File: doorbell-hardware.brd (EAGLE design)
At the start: 100 x 80 mm, 14 parts, among them T1 BC846

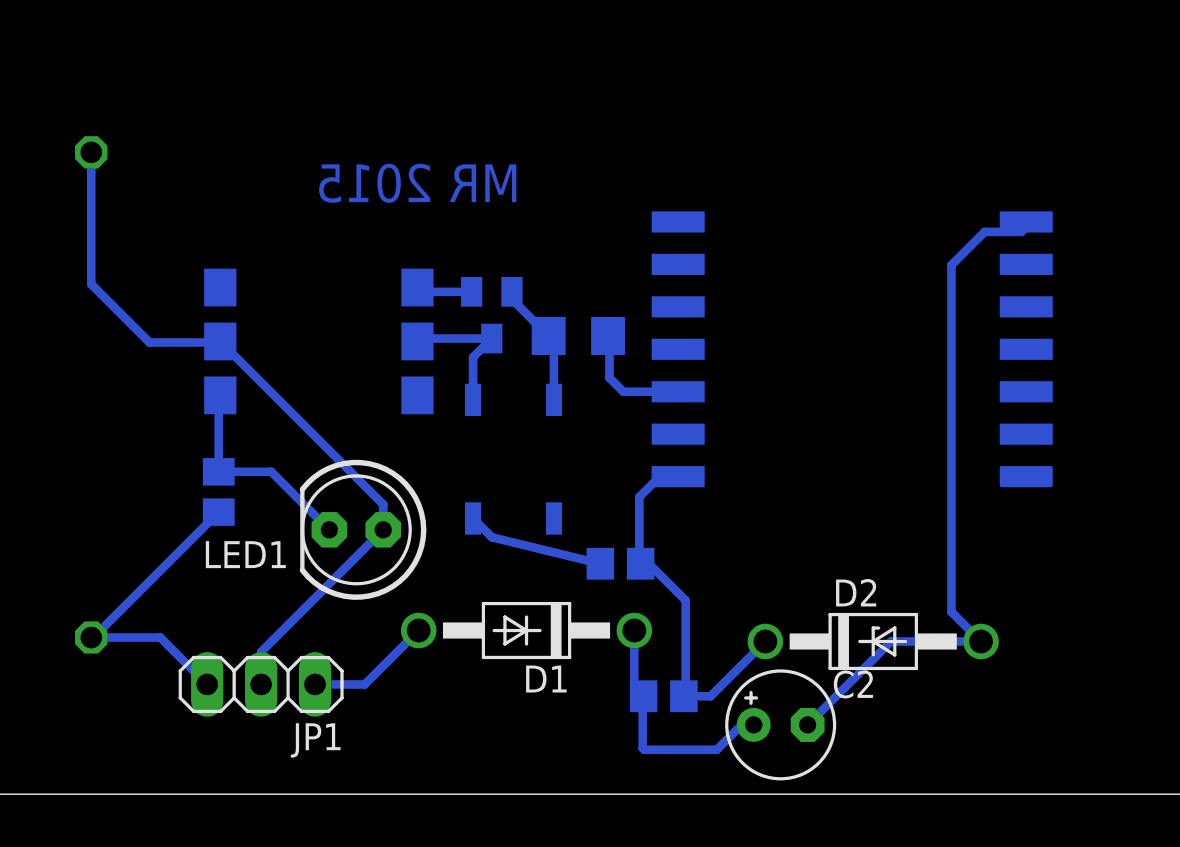
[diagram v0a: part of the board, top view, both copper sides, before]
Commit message: Replaced zener with ldo, started work on sleep and interrupt
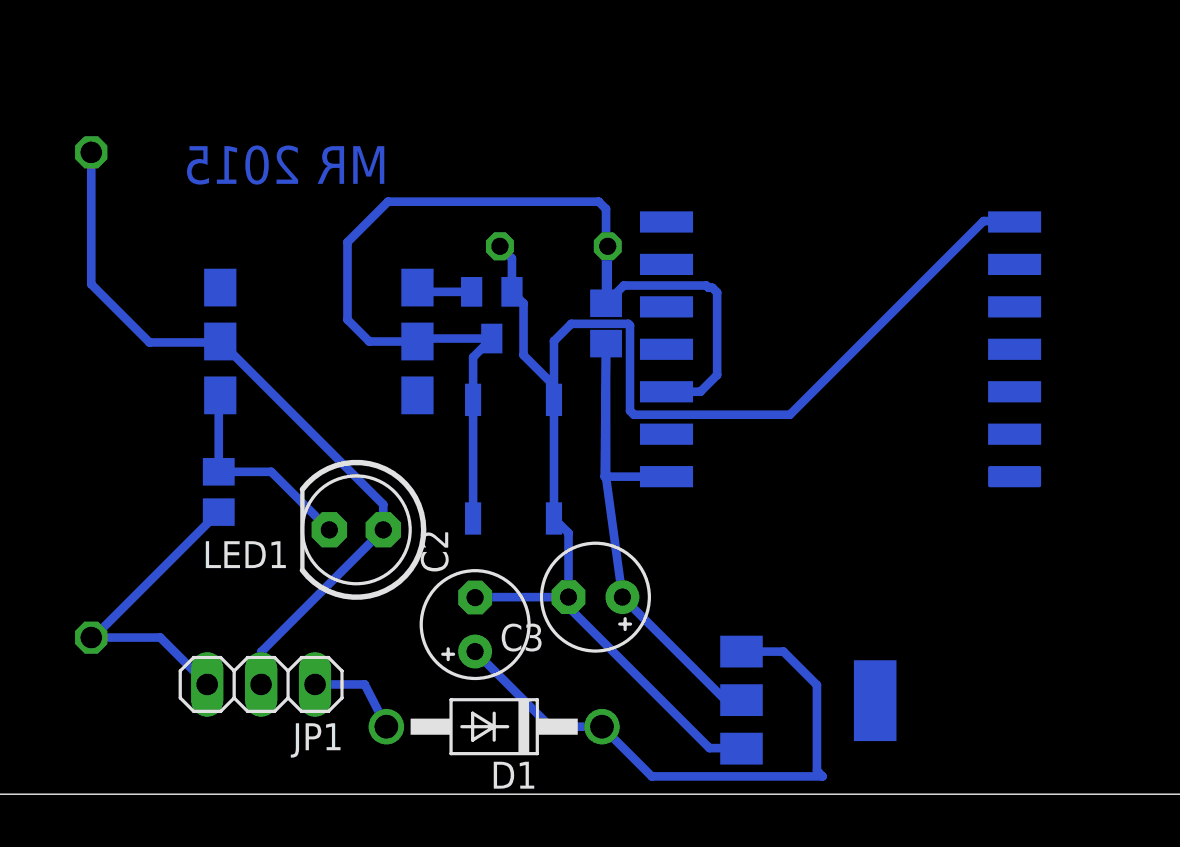
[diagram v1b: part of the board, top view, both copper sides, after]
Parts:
- removed D2: 1N4728, diode:DO41Z10
- removed R2: (no value), eagle-ltspice:R0805
- added C3: 100u, rcl:E2,5-5
- added IC1: REG1117, burr-brown:SOT223
- C1: value (none) -> 10u; device rcl:C1206 -> rcl:C050-024X044
- C2: value (none) -> 10u
- R4: value 1k -> 10k
- moved C2 15.2 mm to (23.7, 7.99), turned to 90 degrees
- moved R4 11.3 mm to (29.9, 22.2), turned to 270 degrees
- moved D1 4.78 mm to (24.6, 3.18)
- moved C1 4.38 mm to (27.4, 25.8)
- moved U$1 0.55 mm to (40.9, 21.8)
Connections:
- removed net N$5: OK1.5, R4.1, S1.3, S1.4, T1.3
- removed net N$6: C1.1, S1.1, S1.2, T1.2
- net BUTTON: now also OK1.5, R4.1, S1.3, S1.4, T1.3
- net GND: now also C1.1, C3.-, IC1.1, S1.1, S1.2, T1.2; no longer D2.A
- net N$1: now also IC1.3; no longer R2.2
- net VCC: now also C3.+, IC1.2; no longer D2.C, R2.1
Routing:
- net BUTTON: track 5.51 -> 52.7 mm
- net GND: track 32.6 -> 66.4 mm
- net N$1: track 11.5 -> 27.4 mm
- net N$5: track 13.3 -> 0.00 mm
- net VCC: track 17.9 -> 28.8 mm
- net N$6: track 5.91 -> 0.00 mm
- net AC+: track 5.94 -> 4.58 mm

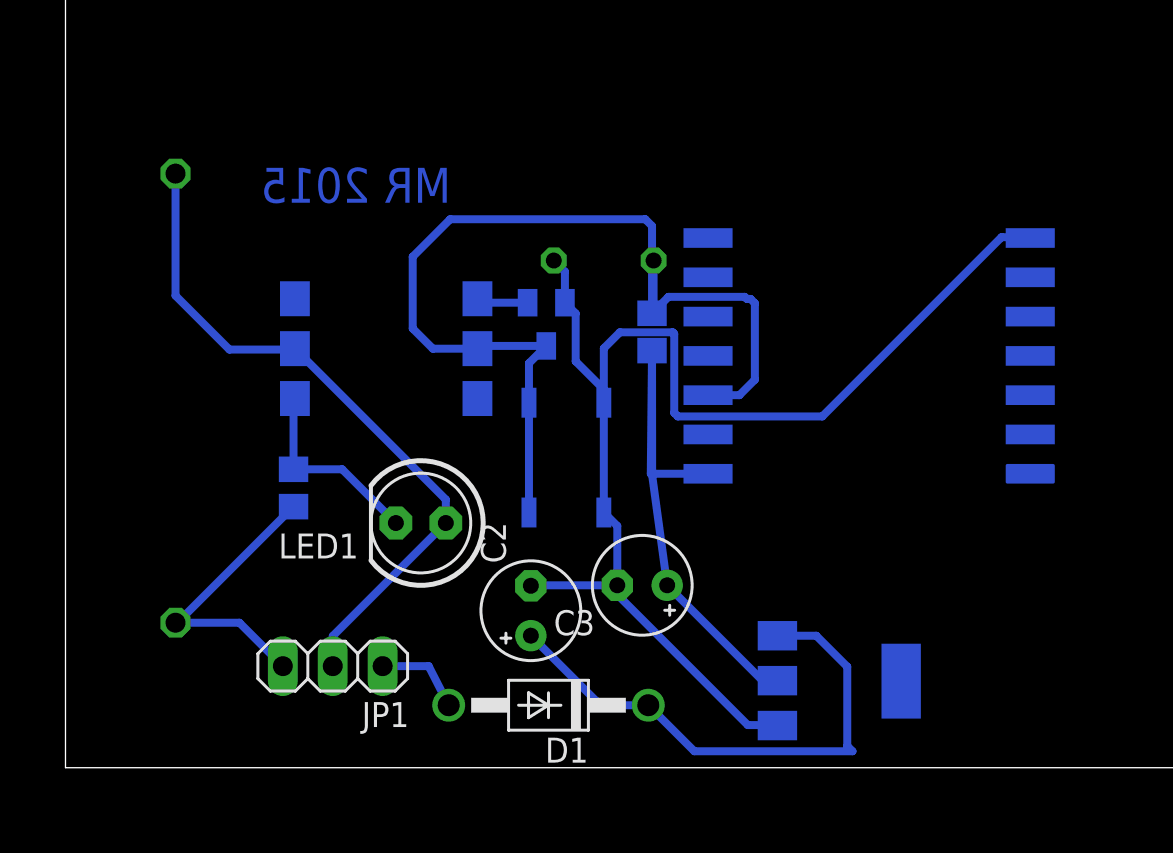
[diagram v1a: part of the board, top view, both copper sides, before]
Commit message: simplified circuit and code
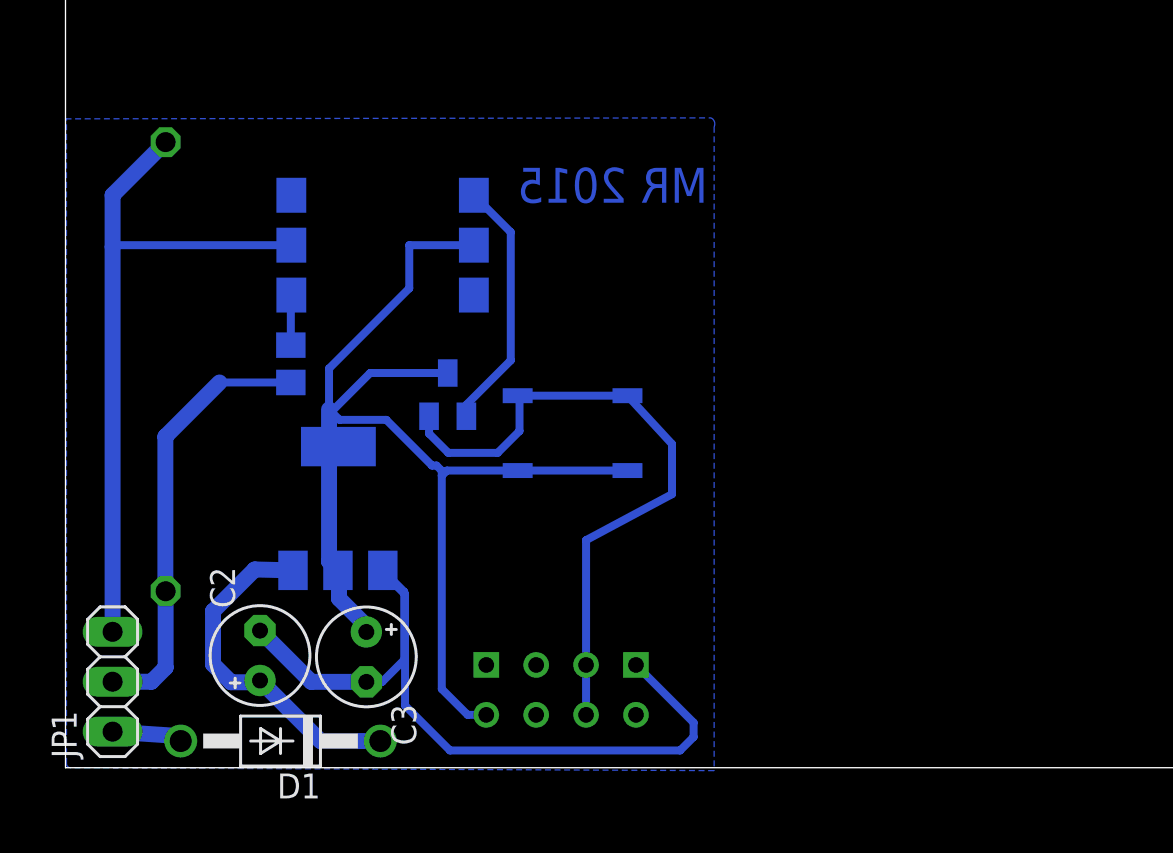
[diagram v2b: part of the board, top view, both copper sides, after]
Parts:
- removed C1: 10u, rcl:C050-024X044
- removed LED1: (no value), adafruit:LED5MM
- removed R4: 10k, eagle-ltspice:R0805
- U$1: value ESP07 -> ESP01; device esp8266modules:ESP07 -> esp8266modules:ESP01
- moved IC1 27.0 mm to (13.9, 13.2), turned to 0 degrees
- moved U$1 19.1 mm to (25.2, 10.9), turned to 0 degrees
- moved C3 14.5 mm to (15.3, 5.64), turned to 270 degrees
- moved C2 14.0 mm to (9.90, 5.71)
- moved D1 13.8 mm to (10.9, 1.36)
- moved JP1 11.2 mm to (2.40, 4.38), turned to 90 degrees
- moved R3 6.32 mm to (11.5, 20.6)
- moved T1 6.16 mm to (19.5, 19.0), turned to 0 degrees
- moved OK1 5.27 mm to (16.1, 26.6)
- moved R1 1.68 mm to (5.10, 20.4)
- moved S1 1.28 mm to (25.8, 17.0), turned to 0 degrees
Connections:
- net AC-: now also JP1.2; no longer JP1.3
- net BUTTON: now also S1.1, S1.2, T1.2, U$1.CH_PD, U$1.GPIO2; no longer C1.2, OK1.5, R4.1, S1.3, S1.4, T1.3, U$1.GPIO12
- net GND: no longer C1.1, S1.1, S1.2, T1.2
- net N$2: now also JP1.3; no longer JP1.2, LED1.A
- net N$3: no longer LED1.K
- net VCC: now also OK1.5, S1.3, S1.4, T1.3; no longer R4.2
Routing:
- net VCC: track 28.8 -> 62.7 mm
- net GND: track 66.4 -> 42.0 mm
- net BUTTON: track 52.7 -> 33.5 mm
- net N$4: track 2.64 -> 13.0 mm
- net N$1: track 27.4 -> 17.9 mm
- net AC-: track 14.8 -> 22.8 mm
- net N$3: track 9.97 -> 2.56 mm
- net AC+: track 4.58 -> 3.84 mm
- added copper zone on layer 16, net N$5

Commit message: Working schematic and smaller layout
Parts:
- removed C3: 100u, rcl:E2,5-5
- removed IC1: REG1117, burr-brown:SOT223
- removed S1: TAC_SWITCHSMD, SparkFun-Electromechanical:TACTILE-SWITCH-SMD
- added C1: 220u, resistor:E2-4
- added D2: 1N4148DO35-7, diode:DO35-7
- added JP2: (no value), pinhead:1X02
- added R2: 1.2k, resistor:0204/5
- C2: value 10u -> 0.1u; device rcl:E2,5-5 -> capacitor-wima:C2.5-2
- D1: value 1N4004 -> BAT49
- JP1: device pinhead:1X03 -> pinhead:1X02
- R1: value 2.4 -> 56k; device resistor:0922/22 -> resistor:0204/5
- R3: value 1k -> 2.4; device eagle-ltspice:R0805 -> resistor:P0613/15
- moved D1 22.3 mm to (6.44, 23.2), turned to 270 degrees
- moved R1 12.6 mm to (10.2, 8.89), flipped to the top, turned to 90 degrees
- moved U$1 12.4 mm to (12.9, 9.44)
- moved R3 10.3 mm to (2.59, 25.7), flipped to the top
- moved T1 9.34 mm to (10.9, 15.2)
- moved JP1 6.82 mm to (1.62, 11.2)
- moved C2 6.79 mm to (14.3, 10.8), turned to 270 degrees
- moved OK1 1.69 mm to (14.5, 26.6), turned to 180 degrees
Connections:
- removed net AC+: D1.A, JP1.1
- removed net AC-: JP1.2, R1.2, R3.2
- new net N$6: C2.1, OK1.4, R2.2, T1.1
- new net N$9: D2.A, U$1.GPIO2
- net BUTTON: now also D2.C, R1.1; no longer S1.1, S1.2, T1.2, U$1.GPIO2
- net GND: now also C2.2, JP2.1, R2.1; no longer C2.-, C3.-, IC1.1
- net N$1: now also D1.A, JP1.2, R3.2; no longer C2.+, D1.C, IC1.3
- net N$2: now also R1.2, T1.2; no longer JP1.3, OK1.2, R1.1
- net N$3: now also C1.+, D1.C; no longer R3.1
- net N$4: now also C1.-, JP1.1, OK1.2, R3.1; no longer OK1.4, T1.1
- net VCC: now also JP2.2; no longer C3.+, IC1.2, S1.3, S1.4
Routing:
- net N$2: track 35.2 -> 2.67 mm
- net VCC: track 62.7 -> 31.9 mm
- net N$4: track 13.0 -> 40.5 mm
- net AC-: track 22.8 -> 0.00 mm
- net BUTTON: track 33.5 -> 16.9 mm
- net N$6: track 0.00 -> 16.6 mm
- net GND: track 42.0 -> 31.2 mm
- net N$1: track 17.9 -> 9.87 mm
- net N$9: track 0.00 -> 7.64 mm
- net N$3: track 2.56 -> 7.99 mm
- net AC+: track 3.84 -> 0.00 mm
- removed copper zone on layer 16, net N$5
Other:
- board size 100 x 80 mm -> 20.5 x 35.1 mm
